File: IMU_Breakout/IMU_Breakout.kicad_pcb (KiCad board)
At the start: 2 copper layers, 10 x 16.8 mm, 4 parts, among them J1 IMU_Connector, U1 LSM6DSL

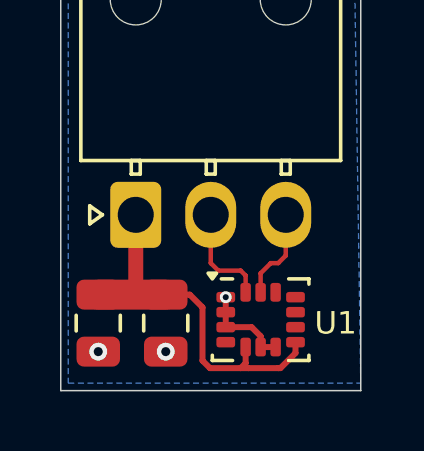
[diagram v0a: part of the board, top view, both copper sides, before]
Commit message: Made Mag compact
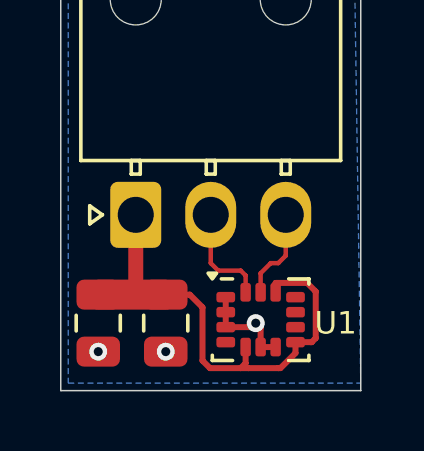
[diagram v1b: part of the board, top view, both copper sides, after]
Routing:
- net /LDO_1.8V: track 13.8 -> 17.9 mm
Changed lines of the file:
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@@
+	)
+	(segment
+		(start 150.75 95)
+		(end 150.75 93.447068)
+		(width 0.2)
+		(layer "F.Cu")
+		(net 2)
 	)
 	(segment
@@
 	)
 	(segment
+		(start 150.75 93.447068)
+		(end 150.462932 93.16)
+		(width 0.2)
+		(layer "F.Cu")
+		(net 2)
+	)
+	(segment
 		(start 146.975 93.975)
 		(end 146.55 93.55)
@@
 	)
 	(segment
+		(start 149.412501 93.16)
+		(end 149.4125 93.160001)
+		(width 0.2)
+		(layer "F.Cu")
+		(net 2)
+	)
+	(segment
 		(start 146.975 95.75)
 		(end 146.975 93.975)
@@
 	)
 	(segment
+		(start 150.615 95.135)
+		(end 150.75 95)
+		(width 0.2)
+		(layer "F.Cu")
+		(net 2)
+	)
+	(segment
+		(start 150.462932 93.16)
+		(end 149.412501 93.16)
+		(width 0.2)
+		(layer "F.Cu")
+		(net 2)
+	)
+	(segment
 		(start 148.5 96)
 		(end 148.25 96)
@@
 	)
 	(segment
+		(start 149.4125 93.160001)
+		(end 149.4125 93.4725)
+		(width 0.2)
+		(layer "F.Cu")
+		(net 2)
+	)
+	(segment
 		(start 148.25 96)
 		(end 147.225 96)
@@
 	)
 	(segment
+		(start 150.075 95.135)
+		(end 150.615 95.135)
+		(width 0.2)
+		(layer "F.Cu")
+		(net 2)
+	)
+	(segment
 		(start 148.4125 95.8375)
 		(end 148.25 96)
@@
 	)
 	(segment
-		(start 148.9125 95.2975)
-		(end 148.9125 94.934568)
+		(start 147.75 94.635)
+		(end 148.615 94.635)
+		(width 0.2)
+		(layer "F.Cu")
+		(net 4)
+	)
+	(segment
+		(start 148.615 94.635)
+		(end 148.75 94.5)
 		(width 0.2)
 		(layer "F.Cu")
@@
 	)
 	(segment
-		(start 148.9125 94.934568)
-		(end 148.612932 94.635)
+		(start 148.9125 95.2975)
+		(end 148.9125 94.6625)
 		(width 0.2)
 		(layer "F.Cu")
@@
 	)
 	(segment
-		(start 148.612932 94.635)
-		(end 147.75 94.635)
-		(width 0.2)
-		(layer "F.Cu")
-		(net 4)
-	)
-	(via
-		(at 147.75 93.635)
-		(size 0.4)
-		(drill 0.2)
-		(layers "F.Cu" "B.Cu")
+		(start 148.9125 94.6625)
+		(end 148.75 94.5)
+		(width 0.2)
+		(layer "F.Cu")
 		(net 4)
 	)
@@
 		(size 0.6)
 		(drill 0.3)
+		(layers "F.Cu" "B.Cu")
+		(net 4)
+	)
+	(via
+		(at 148.75 94.5)
+		(size 0.6)
+		(drill 0.3)

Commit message: Switched connectors
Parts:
- J1: footprint Connector_Molex:Molex_Nano-Fit_105313-xx03_1x03_P2.50mm_Horizontal -> UTSVT_Connectors:Molex_MicroFit3.0_1x3xP3.00mm_PolarizingPeg_Vertical
- moved J1 6.21 mm to (150.8, 89.3), turned to 180 degrees
- moved C1 5.05 mm to (148.5, 93.8)
- moved C2 5.05 mm to (150.8, 93.8)
- moved U1 3.57 mm to (145.4, 93.7)
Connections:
- J1 pad 2: /IMU_I2C_SDA -> /IMU_I2C_SCL
- J1 pad 3: /IMU_I2C_SCL -> /IMU_I2C_SDA
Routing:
- net /LDO_1.8V: track 17.9 -> 12.5 mm
- net /IMU_I2C_SCL: track 2.97 -> 5.18 mm
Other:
- board size 10 x 16.8 mm -> 15.5 x 9.8 mm

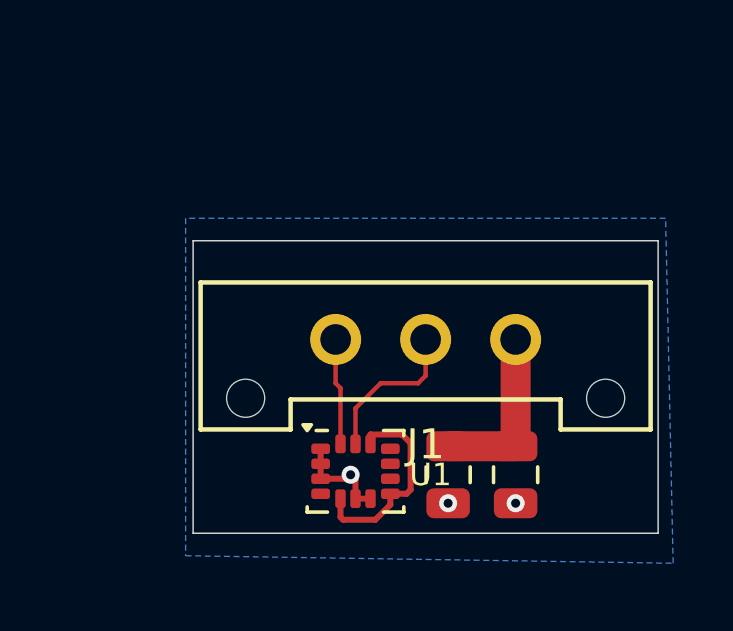
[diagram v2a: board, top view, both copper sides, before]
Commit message: Switched LDO Caps
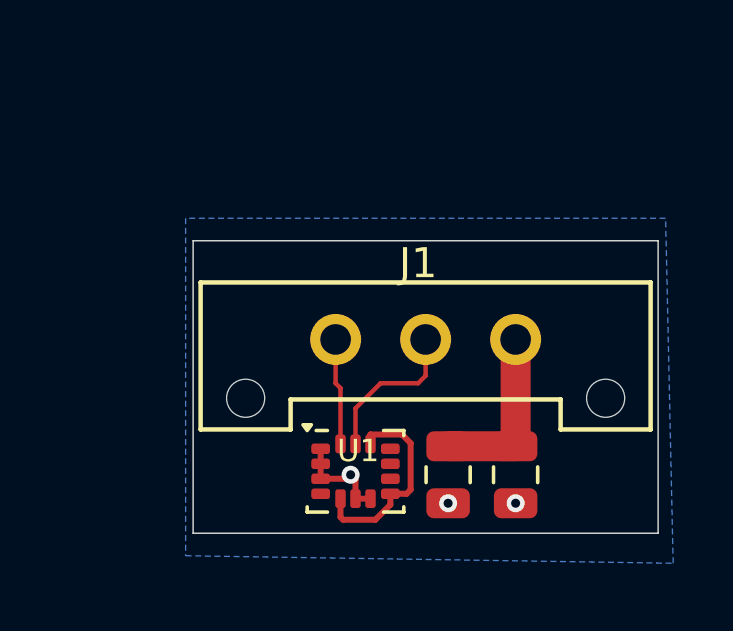
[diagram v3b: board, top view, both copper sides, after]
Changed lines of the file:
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@@
 		(tags "LGA NoLead")
 		(property "Reference" "U1"
-			(at 2.5 0.115 0)
+			(at 0.0875 -0.685 0)
 			(layer "F.SilkS")
 			(effects
@@
 		(at 150.75 89.29 180)
 		(property "Reference" "J1"
-			(at 3 -3.5 360)
-			(layer "F.SilkS")
-			(effects
+			(at 3.25 2.54 360)
+			(layer "F.SilkS")
+			(effects

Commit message: Approved Connectors and gnd connected
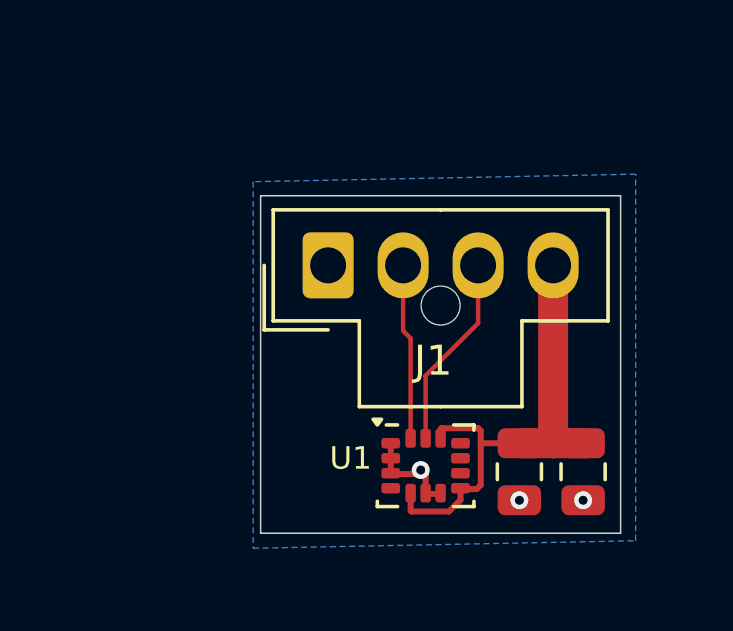
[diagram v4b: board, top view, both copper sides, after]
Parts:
- J1: value IMU_Connector -> Conn_01x04_Socket; footprint UTSVT_Connectors:Molex_MicroFit3.0_1x3xP3.00mm_PolarizingPeg_Vertical -> Connector_Molex:Molex_Nano-Fit_105309-xx04_1x04_P2.50mm_Vertical
- moved J1 6.72 mm to (144.5, 86.8), turned to 90 degrees
- moved C1 2.38 mm to (150.9, 93.7)
- moved U1 2.34 mm to (147.8, 93.5)
- moved C2 2.25 mm to (153.0, 93.7)
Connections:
- C1 pad 1: /LDO_1.8V -> +1V8
- C2 pad 1: /LDO_1.8V -> +1V8
- J1 pad 1: /LDO_1.8V -> GND
- J1 pad 2: /IMU_I2C_SCL -> /IMU_I2C_SDA
- J1 pad 3: /IMU_I2C_SDA -> /IMU_I2C_SCL
- U1 pad 12: /LDO_1.8V -> +1V8
- U1 pad 5: /LDO_1.8V -> +1V8
- U1 pad 8: /LDO_1.8V -> +1V8
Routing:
- net +1V8: track 0.00 -> 16.5 mm
- net /LDO_1.8V: track 12.5 -> 0.00 mm
- net /IMU_I2C_SDA: track 3.55 -> 6.12 mm
- net /IMU_I2C_SCL: track 5.18 -> 6.74 mm
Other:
- board size 15.5 x 9.8 mm -> 12 x 11.2 mm

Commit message: made cuter and added silkscreens
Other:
- board text added: "IMU CONN"
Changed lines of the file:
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@@
 		)
 		(fp_text user "${REFERENCE}"
-			(at 1.1 3.75 360)
+			(at 1.1 3.75 0)
 			(layer "F.Fab")
 			(effects
@@
 			(pintype "passive")
 		)
-		(model "${KICAD8_3DMODEL_DIR}/Connector_Molex.3dshapes/Molex_Nano-Fit_105309-xx04_1x04_P2.50mm_Vertical.wrl"
+		(model "C:/Users/adivp/Desktop/LHR/DataAcq-Speed/3Dmodels/1053092104.stp"
 			(offset
-				(xyz 0 0 0)
+				(xyz 0 -3.75 4.5)
 			)
 			(scale
@@
 			)
 			(rotate
-				(xyz 0 0 0)
+				(xyz 0 0 -90)
 			)
 		)
@@
 		(tags "LGA NoLead")
 		(property "Reference" "U1"
-			(at -2.5 -0.25 0)
+			(at -2.5 0.25 0)
 			(layer "F.SilkS")
 			(effects
@@
 		(layer "Edge.Cuts")
 	)
+	(gr_text "IMU\nCONN"
+		(at 143.75 90 0)
+		(layer "F.SilkS")
+		(effects
+			(font
+				(size 0.5 0.5)
+				(thickness 0.125)
+			)
+		)
+	)
 	(segment

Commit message: made bom
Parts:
- moved U1 1.75 mm to (146.0, 93.5)
- moved C1 1.13 mm to (149.8, 93.8)
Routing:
- net /IMU_I2C_SCL: track 6.74 -> 8.39 mm
- net +1V8: track 16.5 -> 18.0 mm
- added copper zone on F.Cu, net GND
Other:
- board text added: "."
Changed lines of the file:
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@@
 	(footprint "Capacitor_SMD:C_0805_2012Metric"
 		(layer "F.Cu")
-		(at 150.875 93.7 -90)
+		(at 149.75 93.75 -90)
 		(descr "Capacitor SMD 0805 (2012 Metric), square (rectangular) end terminal, IPC_7351 nominal, (Body size source: IPC-SM-782 page 76, https://www.pcb-3d.com/wordpress/wp-content/uploads/ipc-sm-782a_amendment_1_and_2.pdf, https://docs.google.com/spreadsheets/d/1BsfQQcO9C6DZCsRaXUlFlo91Tg2WpOkGARC1WS5S8t0/edit?usp=sharing), generated with kicad-footprint-generator")
 		(tags "capacitor")
@@
 	(footprint "Capacitor_SMD:C_0805_2012Metric"
 		(layer "F.Cu")
-		(at 153 93.7 -90)
+		(at 153 93.75 -90)
 		(descr "Capacitor SMD 0805 (2012 Metric), square (rectangular) end terminal, IPC_7351 nominal, (Body size source: IPC-SM-782 page 76, https://www.pcb-3d.com/wordpress/wp-content/uploads/ipc-sm-782a_amendment_1_and_2.pdf, https://docs.google.com/spreadsheets/d/1BsfQQcO9C6DZCsRaXUlFlo91Tg2WpOkGARC1WS5S8t0/edit?usp=sharing), generated with kicad-footprint-generator")
 		(tags "capacitor")
@@
 	(footprint "Package_LGA:LGA-14_3x2.5mm_P0.5mm_LayoutBorder3x4y"
 		(layer "F.Cu")
-		(at 147.75 93.5)
+		(at 146 93.5)
 		(descr "LGA, 14 Pin (https://www.st.com/resource/en/datasheet/lsm6ds3tr-c.pdf), generated with kicad-footprint-generator ipc_noLead_generator.py")
 		(tags "LGA NoLead")
 		(property "Reference" "U1"
-			(at -2.5 0.25 0)
+			(at -9.5 -1.75 0)
 			(layer "F.SilkS")
 			(effects
@@
 	)
 	(gr_text "IMU\nCONN"
-		(at 143.75 90 0)
+		(at 152.6 90 0)
 		(layer "F.SilkS")
 		(effects
 			(font
-				(size 0.5 0.5)
-				(thickness 0.125)
-			)
-		)
-	)
-	(segment
-		(start 147.75 92.5875)
-		(end 147.75 90.5)
+				(size 0.8 0.8)
+				(thickness 0.15)
+				(bold yes)
+			)
+		)
+	)
+	(gr_text "."
+		(at 144 88.6 0)
+		(layer "F.SilkS")
+		(effects
+			(font
+				(size 1.5 1.5)
+				(thickness 0.3)
+				(bold yes)
+			)
+			(justify left bottom)
+		)
+	)
+	(segment
+		(start 146 92.5875)
+		(end 146 91.5)
 		(width 0.15)
 		(layer "F.Cu")
@@
 	)
 	(segment
-		(start 149.5 88.75)
-		(end 149.5 86.57)
+		(start 149.5 90)
+		(end 149 90.5)
 		(width 0.15)
 		(layer "F.Cu")
@@
 	)
 	(segment
-		(start 147.75 90.5)
-		(end 149.5 88.75)
+		(start 149.5 86.82)
+		(end 149.5 90)
 		(width 0.15)
 		(layer "F.Cu")
@@
 	)
 	(segment
-		(start 147.25 89.25)
-		(end 147 89)
+		(start 146 91.5)
+		(end 147 90.5)
 		(width 0.15)
 		(layer "F.Cu")
+		(net 1)
+	)
+	(segment
+		(start 147 90.5)
+		(end 149 90.5)
+		(width 0.15)
+		(layer "F.Cu")
+		(net 1)
+	)
+	(segment
+		(start 147 90)
+		(end 147 86.82)
+		(width 0.15)
+		(layer "F.Cu")
 		(net 2)
 	)
 	(segment
-		(start 147.25 92.5875)
-		(end 147.25 89.25)
+		(start 145.5 92.5875)
+		(end 145.5 91.5)
 		(width 0.15)
 		(layer "F.Cu")
@@
 	)
 	(segment
-		(start 147 89)
-		(end 147 86.57)
+		(start 145.5 91.5)
+		(end 147 90)
 		(width 0.15)
 		(layer "F.Cu")
@@
 	)
 	(segment
-		(start 146.5875 93.7775)
-		(end 147.4525 93.7775)
+		(start 146.5 94.44)
+		(end 146 94.44)
 		(width 0.2)
 		(layer "F.Cu")
@@
 	)
 	(segment
-		(start 147.4525 93.7775)
-		(end 147.5875 93.6425)
+		(start 145.85 93.75)
+		(end 146 93.6)
+		(width 0.15)
+		(layer "F.Cu")
+		(net 3)
+	)
+	(segment
+		(start 144.8375 93.75)
+		(end 145.85 93.75)
+		(width 0.15)
+		(layer "F.Cu")
+		(net 3)
+	)
+	(segment
+		(start 146 94.4125)
+		(end 146 93.6)
+		(width 0.15)
+		(layer "F.Cu")
+		(net 3)
+	)
+	(segment
+		(start 144.8375 93.7775)
+		(end 144.8375 92.7775)
 		(width 0.2)
 		(layer "F.Cu")
-		(net 3)
-	)
-	(segment
-		(start 148.25 94.44)
-		(end 147.75 94.44)
-		(width 0.2)
-		(layer "F.Cu")
-		(net 3)
-	)
-	(segment
-		(start 147.75 94.44)
-		(end 147.75 93.805)
-		(width 0.2)
-		(layer "F.Cu")
-		(net 3)
-	)
-	(segment
-		(start 146.5875 93.7775)
-		(end 146.5875 92.7775)
-		(width 0.2)
-		(layer "F.Cu")
-		(net 3)
-	)
-	(segment
-		(start 147.75 93.805)
-		(end 147.5875 93.6425)
-		(width 0.2)
-		(layer "F.Cu")
-		(net 3)
-	)
-	(via
-		(at 147.5875 93.6425)
-		(size 0.6)
-		(drill 0.3)
-		(layers "F.Cu" "B.Cu")
 		(net 3)
 	)
@@
 	)
 	(via
-		(at 150.875 94.65)
+		(at 146 93.6)
+		(size 0.6)
+		(drill 0.3)
+		(layers "F.Cu" "B.Cu")
+		(free yes)
+		(net 3)
+	)
+	(via
+		(at 149.75 94.7)
 		(size 0.6)
 		(drill 0.3)
@@
 	)
 	(segment
-		(start 148.9125 94.2775)
-		(end 149.4525 94.2775)
+		(start 149.75 92.8)
+		(end 152.95 92.8)
+		(width 1)
+		(layer "F.Cu")
+		(net 8)
+	)
+	(segment
+		(start 147.1625 94.2775)
+		(end 147.7025 94.2775)
 		(width 0.2)
 		(layer "F.Cu")
@@
 	)
 	(segment
-		(start 147.25 94.4125)
-		(end 147.25 95)
+		(start 145.5 94.4125)
+		(end 145.5 95)
 		(width 0.2)
 		(layer "F.Cu")
@@
 	)
 	(segment
-		(start 149.5875 94.1425)
-		(end 149.5875 92.75)
+		(start 147.8375 94.1425)
+		(end 147.8375 92.75)
 		(width 0.2)
 		(layer "F.Cu")
@@
 	)
 	(segment
-		(start 152 92.75)
-		(end 150.875 92.75)
-		(width 1)
+		(start 145.5 95)
+		(end 145.525 95.025)
+		(width 0.2)
 		(layer "F.Cu")
 		(net 8)
 	)
 	(segment
-		(start 147.25 95)
-		(end 147.275 95.025)
+		(start 147.8875 92.8)
+		(end 147.8375 92.75)
 		(width 0.2)
 		(layer "F.Cu")
@@
 	)
 	(segment
-		(start 149.5 92.25)
-		(end 148.275001 92.25)
+		(start 147.75 92.25)
+		(end 146.525001 92.25)
 		(width 0.2)
 		(layer "F.Cu")
@@
 	)
 	(segment
-		(start 147.275 95.025)
-		(end 148.527932 95.025)
+		(start 145.525 95.025)
+		(end 146.777932 95.025)
 		(width 0.2)
 		(layer "F.Cu")
@@
 	)
 	(segment
-		(start 148.25 92.275001)
-		(end 148.25 92.5875)
+		(start 149.75 92.8)
+		(end 147.8875 92.8)
 		(width 0.2)
 		(layer "F.Cu")
@@
 	)
 	(segment
-		(start 149.5875 92.75)
-		(end 150.875 92.75)
+		(start 146.5 92.275001)
+		(end 146.5 92.5875)
 		(width 0.2)
 		(layer "F.Cu")
@@
 	)
 	(segment
-		(start 148.527932 95.025)
-		(end 148.9125 94.640432)
+		(start 146.777932 95.025)
+		(end 147.1625 94.640432)
 		(width 0.2)
 		(layer "F.Cu")
@@
 	)
 	(segment
-		(start 149.4525 94.2775)
-		(end 149.5875 94.1425)
+		(start 147.7025 94.2775)
+		(end 147.8375 94.1425)
 		(width 0.2)
 		(layer "F.Cu")
@@
 	)
 	(segment
-		(start 148.9125 94.640432)
-		(end 148.9125 94.2775)
+		(start 147.1625 94.640432)
+		(end 147.1625 94.2775)
 		(width 0.2)
 		(layer "F.Cu")
@@
 	)
 	(segment
-		(start 148.275001 92.25)
-		(end 148.25 92.275001)
+		(start 147.8375 92.75)
+		(end 147.8375 92.3375)
 		(width 0.2)
 		(layer "F.Cu")
@@
 	)
 	(segment
-		(start 149.5875 92.75)
-		(end 149.5875 92.3375)
+		(start 147.8375 92.3375)
+		(end 147.75 92.25)
 		(width 0.2)
-		(layer "F.Cu")
-		(net 8)
-	)
-	(segment
-		(start 149.5875 92.3375)
-		(end 149.5 92.25)
-		(width 0.2)
-		(layer "F.Cu")
-		(net 8)
-	)
-	(segment
-		(start 153.125 92.75)
-		(end 152 92.75)
-		(width 1)
 		(layer "F.Cu")
 		(net 8)
@@
 		(net 3)
 		(net_name "GND")
-		(layer "B.Cu")
+		(layers "F&B.Cu")
 		(hatch edge 0.5)
 		(connect_pads
@@
 		(polygon
 			(pts
-				(xy 142 84.030762) (xy 142 96.25) (xy 154.75 96) (xy 154.75 83.780762)
-			)
-		)
+				(xy 142 84.030762) (xy 142 96.25) (xy 154.6 96.2) (xy 154.8 84.1)
+			)
+		)

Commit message: fixed review stuffs
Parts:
- moved C2 1.40 mm to (151.6, 93.8)
- moved C1 0.55 mm to (149.2, 93.8)
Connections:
- net +1V8 renamed +3V3
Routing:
- net +3V3: track 18.0 -> 17.4 mm
- net GND: vias 3 -> 7
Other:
- board size 12 x 11.2 mm -> 12 x 11.8 mm
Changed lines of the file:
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@@
 	(net 6 "unconnected-(U1-INT2-Pad9)")
 	(net 7 "unconnected-(U1-NC-Pad10)")
-	(net 8 "+1V8")
+	(net 8 "+3V3")
 	(footprint "Capacitor_SMD:C_0805_2012Metric"
 		(layer "F.Cu")
-		(at 149.75 93.75 -90)
+		(at 149.2 93.75 -90)
 		(descr "Capacitor SMD 0805 (2012 Metric), square (rectangular) end terminal, IPC_7351 nominal, (Body size source: IPC-SM-782 page 76, https://www.pcb-3d.com/wordpress/wp-content/uploads/ipc-sm-782a_amendment_1_and_2.pdf, https://docs.google.com/spreadsheets/d/1BsfQQcO9C6DZCsRaXUlFlo91Tg2WpOkGARC1WS5S8t0/edit?usp=sharing), generated with kicad-footprint-generator")
 		(tags "capacitor")
@@
 			(layers "F.Cu" "F.Paste" "F.Mask")
 			(roundrect_rratio 0.25)
-			(net 8 "+1V8")
+			(net 8 "+3V3")
 			(pintype "passive")
 		)
@@
 			(layers "*.Cu" "*.Mask")
 			(remove_unused_layers no)
-			(net 8 "+1V8")
+			(net 8 "+3V3")
 			(pinfunction "Pin_4")
 			(pintype "passive")
@@
 	(footprint "Capacitor_SMD:C_0805_2012Metric"
 		(layer "F.Cu")
-		(at 153 93.75 -90)
+		(at 151.6 93.75 -90)
 		(descr "Capacitor SMD 0805 (2012 Metric), square (rectangular) end terminal, IPC_7351 nominal, (Body size source: IPC-SM-782 page 76, https://www.pcb-3d.com/wordpress/wp-content/uploads/ipc-sm-782a_amendment_1_and_2.pdf, https://docs.google.com/spreadsheets/d/1BsfQQcO9C6DZCsRaXUlFlo91Tg2WpOkGARC1WS5S8t0/edit?usp=sharing), generated with kicad-footprint-generator")
 		(tags "capacitor")
@@
 			(layers "F.Cu" "F.Paste" "F.Mask")
 			(roundrect_rratio 0.25)
-			(net 8 "+1V8")
+			(net 8 "+3V3")
 			(pintype "passive")
 		)
@@
 		(tags "LGA NoLead")
 		(property "Reference" "U1"
-			(at -9.5 -1.75 0)
+			(at 0 -0.75 0)
 			(layer "F.SilkS")
 			(effects
@@
 			(layers "F.Cu" "F.Paste" "F.Mask")
 			(roundrect_rratio 0.25)
-			(net 8 "+1V8")
+			(net 8 "+3V3")
 			(pinfunction "VDDIO")
 			(pintype "power_in")
@@
 			(layers "F.Cu" "F.Paste" "F.Mask")
 			(roundrect_rratio 0.25)
-			(net 8 "+1V8")
+			(net 8 "+3V3")
 			(pinfunction "VDD")
 			(pintype "power_in")
@@
 			(layers "F.Cu" "F.Paste" "F.Mask")
 			(roundrect_rratio 0.25)
-			(net 8 "+1V8")
+			(net 8 "+3V3")
 			(pinfunction "CS")
 			(pintype "input")
@@
 	(gr_rect
 		(start 142.25 84.5)
-		(end 154.25 95.75)
+		(end 154.25 96.25)
 		(stroke
 			(width 0.05)
@@
 	)
 	(via
-		(at 153 94.65)
+		(at 151.25 91.5)
 		(size 0.6)
 		(drill 0.3)
 		(layers "F.Cu" "B.Cu")
+		(free yes)
+		(net 3)
+	)
+	(via
+		(at 147 91.5)
+		(size 0.6)
+		(drill 0.3)
+		(layers "F.Cu" "B.Cu")
+		(free yes)
+		(net 3)
+	)
+	(via
+		(at 144.75 91.5)
+		(size 0.6)
+		(drill 0.3)
+		(layers "F.Cu" "B.Cu")
+		(free yes)
+		(net 3)
+	)
+	(via
+		(at 151.6 94.7)
+		(size 0.6)
+		(drill 0.3)
+		(layers "F.Cu" "B.Cu")
+		(net 3)
+	)
+	(via
+		(at 152.75 91.5)
+		(size 0.6)
+		(drill 0.3)
+		(layers "F.Cu" "B.Cu")
+		(free yes)
 		(net 3)
 	)
@@
 	)
 	(via
-		(at 149.75 94.7)
+		(at 149.2 94.7)
 		(size 0.6)
 		(drill 0.3)
@@
 	)
 	(segment
-		(start 149.75 92.8)
-		(end 152.95 92.8)
-		(width 1)
-		(layer "F.Cu")
-		(net 8)
-	)
-	(segment
 		(start 147.1625 94.2775)
 		(end 147.7025 94.2775)
@@
 	)
 	(segment
+		(start 149.75 92.8)
+		(end 151.5 92.8)
+		(width 0.2)
+		(layer "F.Cu")
+		(net 8)
+	)
+	(segment
 		(start 145.5 94.4125)
 		(end 145.5 95)
@@
 	)
 	(segment
-		(start 152 92.75)
-		(end 152 86.82)
-		(width 1)
-		(layer "F.Cu")
-		(net 8)
-	)
-	(segment
 		(start 147.75 92.25)
 		(end 146.525001 92.25)
@@
 	)
 	(segment
+		(start 152 92)
+		(end 152 92.8)
+		(width 0.2)
+		(layer "F.Cu")
+		(net 8)
+	)
+	(segment
+		(start 152 92.3)
+		(end 152 92)
+		(width 0.2)
+		(layer "F.Cu")
+		(net 8)
+	)
+	(segment
 		(start 147.7025 94.2775)
 		(end 147.8375 94.1425)
@@
 		(start 147.1625 94.640432)
 		(end 147.1625 94.2775)
+		(width 0.2)
+		(layer "F.Cu")
+		(net 8)
+	)
+	(segment
+		(start 151.5 92.8)
+		(end 152 92.8)
+		(width 0.2)
+		(layer "F.Cu")
+		(net 8)
+	)
+	(segment
+		(start 152 92)
+		(end 152 86.82)
 		(width 0.2)
 		(layer "F.Cu")
@@
 		(hatch edge 0.5)
 		(connect_pads
-			(clearance 0.5)
-		)
-		(min_thickness 0.25)
+			(clearance 0.3)
+		)
+		(min_thickness 0.15)
 		(filled_areas_thickness no)
 		(fill yes
-			(thermal_gap 0.5)
-			(thermal_bridge_width 0.5)
+			(thermal_gap 0.4)
+			(thermal_bridge_width 0.25)
 		)
 		(polygon
 			(pts
-				(xy 142 84.030762) (xy 142 96.25) (xy 154.6 96.2) (xy 154.8 84.1)
-			)
-		)
+				(xy 142 84.030762) (xy 142 97) (xy 155 97) (xy 154.8 84.1)
+			)
+		)

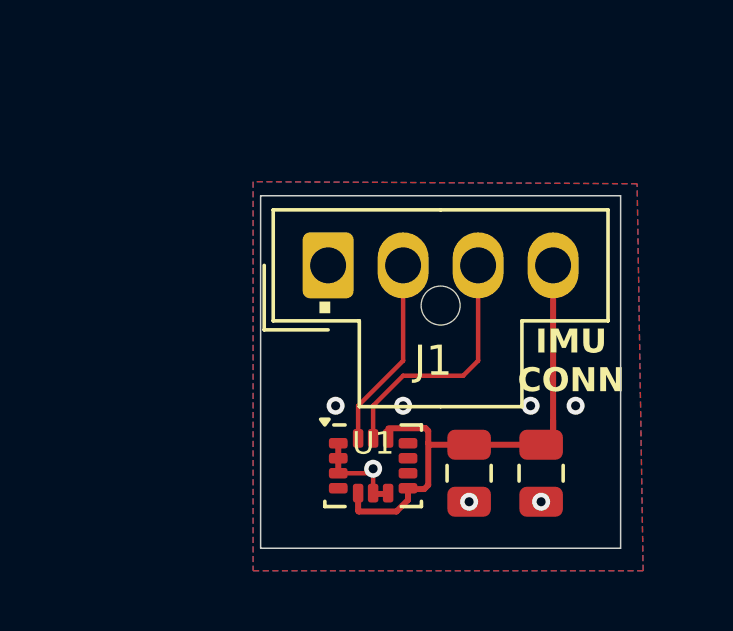
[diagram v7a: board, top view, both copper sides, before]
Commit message: fixed imu connector oops
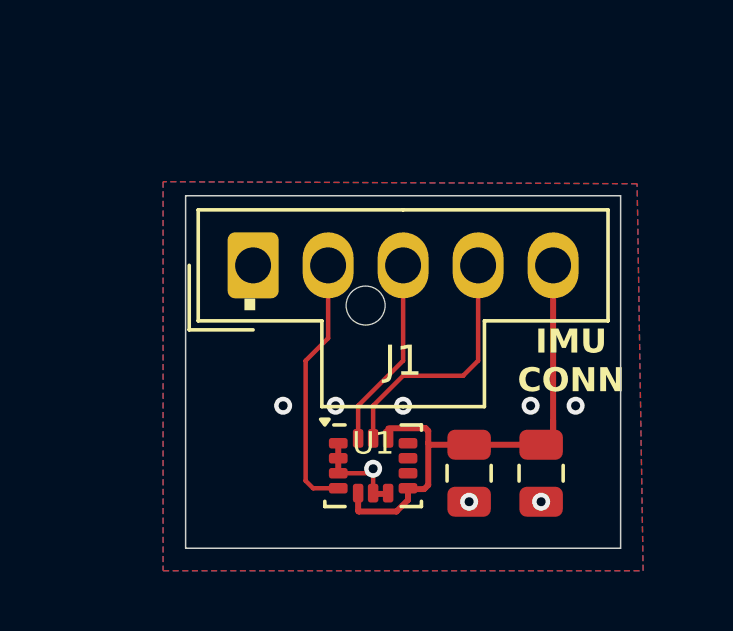
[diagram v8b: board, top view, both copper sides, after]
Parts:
- J1: value Conn_01x04_Socket -> Conn_01x05_Socket; footprint Connector_Molex:Molex_Nano-Fit_105309-xx04_1x04_P2.50mm_Vertical -> Connector_Molex:Molex_Nano-Fit_105309-xx05_1x05_P2.50mm_Vertical
- moved J1 2.50 mm to (142.0, 86.8)
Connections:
- J1 pad 2: /IMU_I2C_SDA -> /IMU_INT
- J1 pad 3: /IMU_I2C_SCL -> /IMU_I2C_SDA
- J1 pad 4: +3V3 -> /IMU_I2C_SCL
- U1 pad 4: unconnected-(U1-INT1-Pad4) -> /IMU_INT
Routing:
- net /IMU_INT: track 0.00 -> 8.68 mm
- net GND: vias 7 -> 8
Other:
- board size 12 x 11.8 mm -> 14.5 x 11.8 mm
